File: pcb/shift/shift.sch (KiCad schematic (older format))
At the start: 7 parts, among them J1 Conn_01x03, U1 74LS595

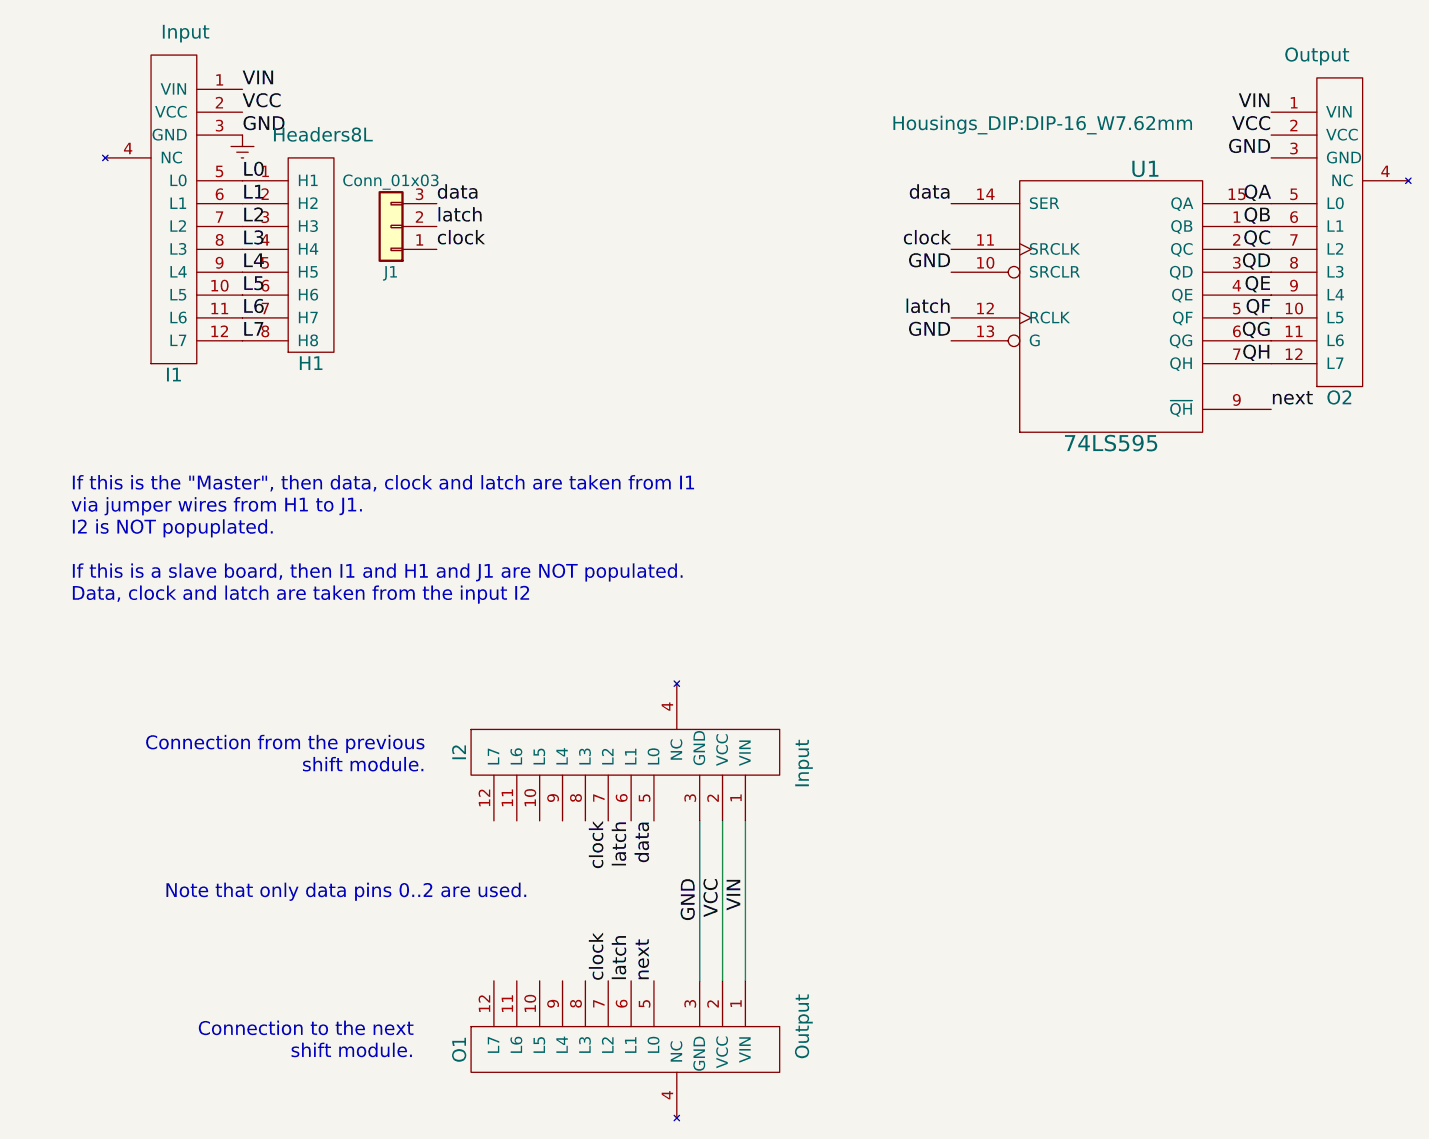
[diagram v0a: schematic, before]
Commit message: Rotated the shift register, re-routed the power lines, and added the option of output-enable.
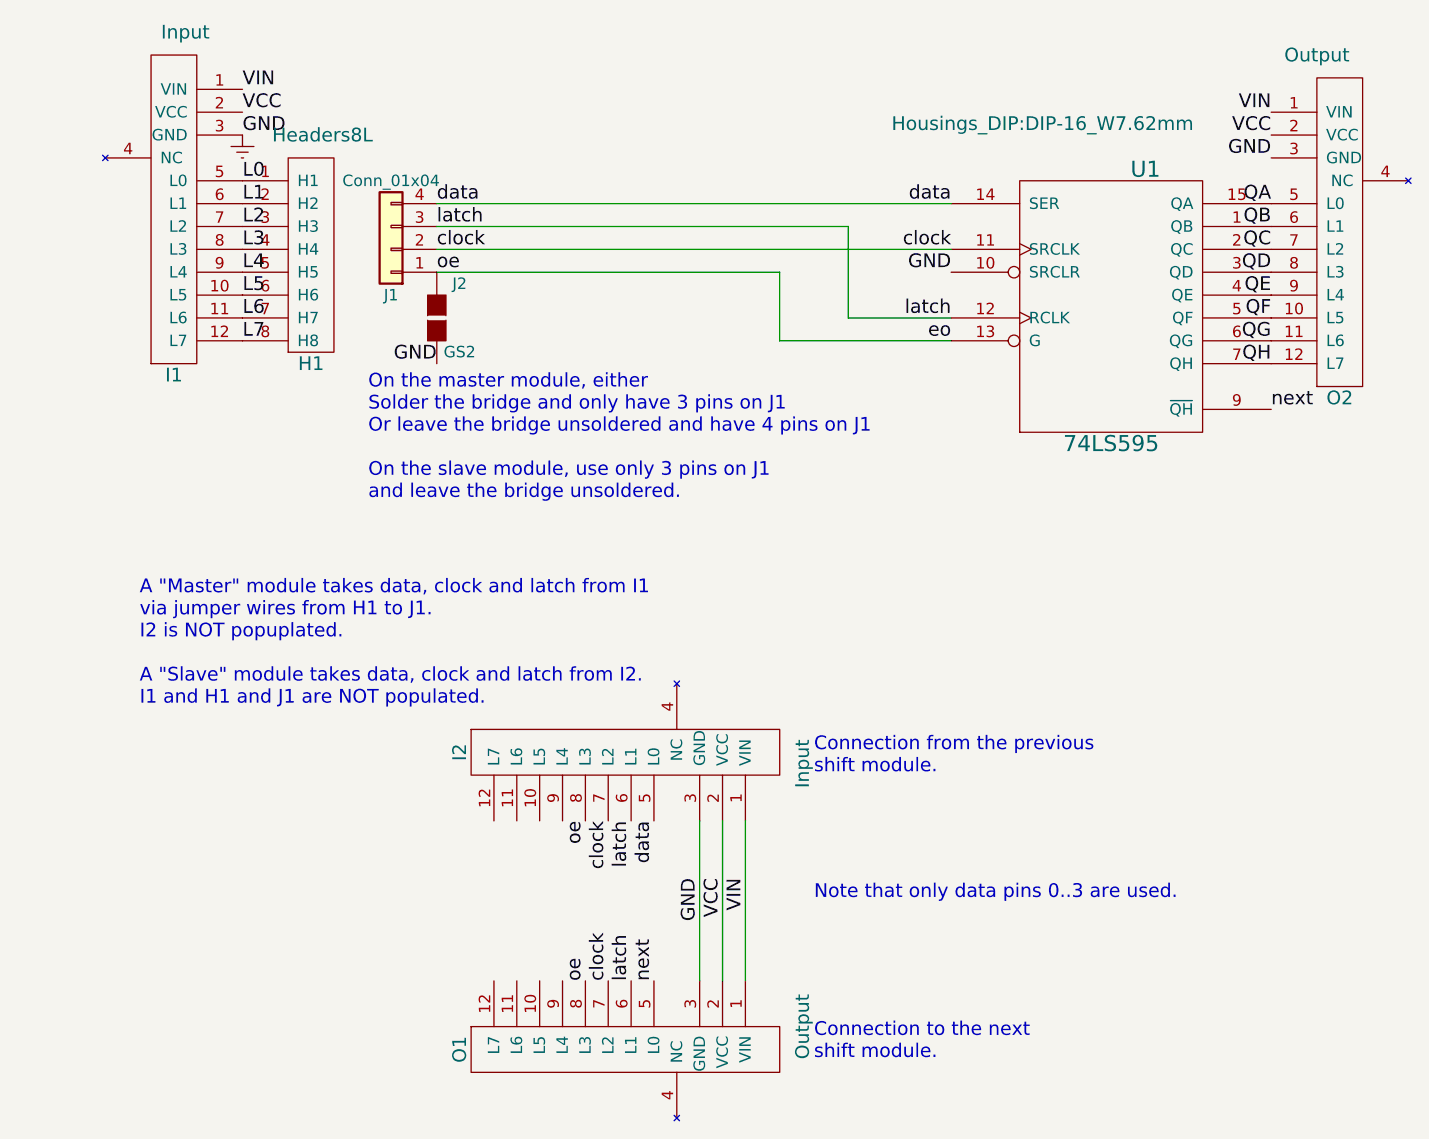
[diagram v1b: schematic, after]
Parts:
- removed J1: Conn_01x03, Pin_Headers:Pin_Header_Straight_1x03_Pitch2.54mm, symbol Conn_01x03
- added J1: Conn_01x04, Pin_Headers:Pin_Header_Straight_1x04_Pitch2.54mm, symbol Conn_01x04
- added J2: GS2, Connectors:GS2, symbol GS2
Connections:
- net Earth: now also J2.2 (G2); no longer U1.13 (G)
- net clock: now also J1.2 (Pin_2)
- net data: now also J1.4 (Pin_4)
- net latch: now also J1.3 (Pin_3)
- net eo: now reaches O1.8 (L3)
- net eo: now also I2.8 (L3), U1.13 (G), J1.1 (Pin_1), J2.1 (G1)
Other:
- note added: "A "Master" module takes data, clock and latch from I1\nvia jumper wires from H1 to J1.\nI2 is NOT popuplated.\n\nA "Slave" module takes data, clock and latch from I2.\nI1 and H1 and J1 are NOT populated.\n"
- note added: "Note that only data pins 0..3 are used."
- note added: "On the master module, either\nSolder the bridge and only have 3 pins on J1\nOr leave the bridge unsoldered and have 4 pins on J1\n\nOn the slave module, use only 3 pins on J1\nand leave the bridge unsoldered."
- note removed: "If this is the "Master", then data, clock and latch are taken from I1\nvia jumper wires from H1 to J1.\nI2 is NOT popuplated.\n\nIf this is a slave board, then I1 and H1 and J1 are NOT populated.\nData, clock and latch are taken from the input I2"
- note removed: "Note that only data pins 0..2 are used."
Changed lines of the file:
@@
 GND
 Text Label 5350 3000 2    60   ~ 0
-GND
+eo
 Text Label 5350 2700 2    60   ~ 0
 GND
@@
 $EndComp
 $Comp
-L Conn_01x03 J1
-U 1 1 5AC7586B
-P 2900 2500
-F 0 "J1" H 2900 2700 50  0000 C CNN
-F 1 "Conn_01x03" H 2900 2300 50  0000 C CNN
-F 2 "Pin_Headers:Pin_Header_Straight_1x03_Pitch2.54mm" H 2900 2500 50  0001 C CNN
-F 3 "" H 2900 2500 50  0001 C CNN
-	1    2900 2500
-	-1   0    0    1
-$EndComp
-$Comp
 L Input I2
 U 1 1 5AC76C5E
@@
 Text Label 3950 5100 3    60   ~ 0
 latch
-Text Notes 1500 4150 0    60   ~ 0
-If this is the "Master", then data, clock and latch are taken from I1\nvia jumper wires from H1 to J1.\nI2 is NOT popuplated.\n\nIf this is a slave board, then I1 and H1 and J1 are NOT populated.\nData, clock and latch are taken from the input I2
+Text Notes 1800 4600 0    60   ~ 0
+A "Master" module takes data, clock and latch from I1\nvia jumper wires from H1 to J1.\nI2 is NOT popuplated.\n\nA "Slave" module takes data, clock and latch from I2.\nI1 and H1 and J1 are NOT populated.\n
 Text Label 3100 2400 0    60   ~ 0
 data
@@
 Text Label 3100 2500 0    60   ~ 0
 latch
-Text Notes 3050 4900 2    60   ~ 0
+Text Notes 4750 4900 0    60   ~ 0
 Connection from the previous\nshift module.
-Text Notes 3000 6150 2    60   ~ 0
+Text Notes 4750 6150 0    60   ~ 0
 Connection to the next\nshift module.
-Text Notes 3500 5450 2    60   ~ 0
-Note that only data pins 0..2 are used.
+Text Notes 4750 5450 0    60   ~ 0
+Note that only data pins 0..3 are used.
 Wire Wire Line
 	4450 5800 4450 5100
@@
 Text Label 6750 3100 2    60   ~ 0
 QH
+$Comp
+L Conn_01x04 J1
+U 1 1 5AC767D3
+P 2900 2600
+F 0 "J1" H 2900 2800 50  0000 C CNN
+F 1 "Conn_01x04" H 2900 2300 50  0000 C CNN
+F 2 "Pin_Headers:Pin_Header_Straight_1x04_Pitch2.54mm" H 2900 2600 50  0001 C CNN
+F 3 "" H 2900 2600 50  0001 C CNN
+	1    2900 2600
+	-1   0    0    1
+$EndComp
+Text Label 3100 2700 0    60   ~ 0
+oe
+$Comp
+L GS2 J2
+U 1 1 5AC7691D
+P 3100 2900
+F 0 "J2" H 3200 3050 50  0000 C CNN
+F 1 "GS2" H 3200 2751 50  0000 C CNN
+F 2 "Connectors:GS2" V 3174 2900 50  0001 C CNN
+F 3 "" H 3100 2900 50  0001 C CNN
+	1    3100 2900
+	1    0    0    -1
+$EndComp
+Text Label 3100 3100 2    60   ~ 0
+GND
+Wire Wire Line
+	3100 2700 4600 2700
+Wire Wire Line
+	4600 2700 4600 3000
+Wire Wire Line
+	4600 3000 5350 3000
+Wire Wire Line
+	3100 2500 4900 2500
+Wire Wire Line
+	4900 2500 4900 2900
+Wire Wire Line
+	4900 2900 5350 2900
+Wire Wire Line
+	5350 2600 3100 2600
+Wire Wire Line
+	3100 2400 5350 2400
+Text Label 3750 5100 3    60   ~ 0
+oe
+Text Label 3750 5800 1    60   ~ 0
+oe
+Text Notes 2800 3700 0    60   ~ 0
+On the master module, either\nSolder the bridge and only have 3 pins on J1\nOr leave the bridge unsoldered and have 4 pins on J1\n\nOn the slave module, use only 3 pins on J1\nand leave the bridge unsoldered.
 $EndSCHEMATC
